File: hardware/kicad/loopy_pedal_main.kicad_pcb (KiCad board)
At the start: 2 copper layers, 175 x 118 mm, 88 parts, among them J1 USB_C_Receptacle_USB2.0_16P, J10 Conn_01x02, J2 Barrel_Jack, J3 Conn_01x06, J4 Conn_01x06, J5 Conn_01x08, J6 Conn_02x03_Odd_Even, J7 Conn_02x03_Odd_Even, J8 DIN-5_180degree, J9 DIN-5_180degree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

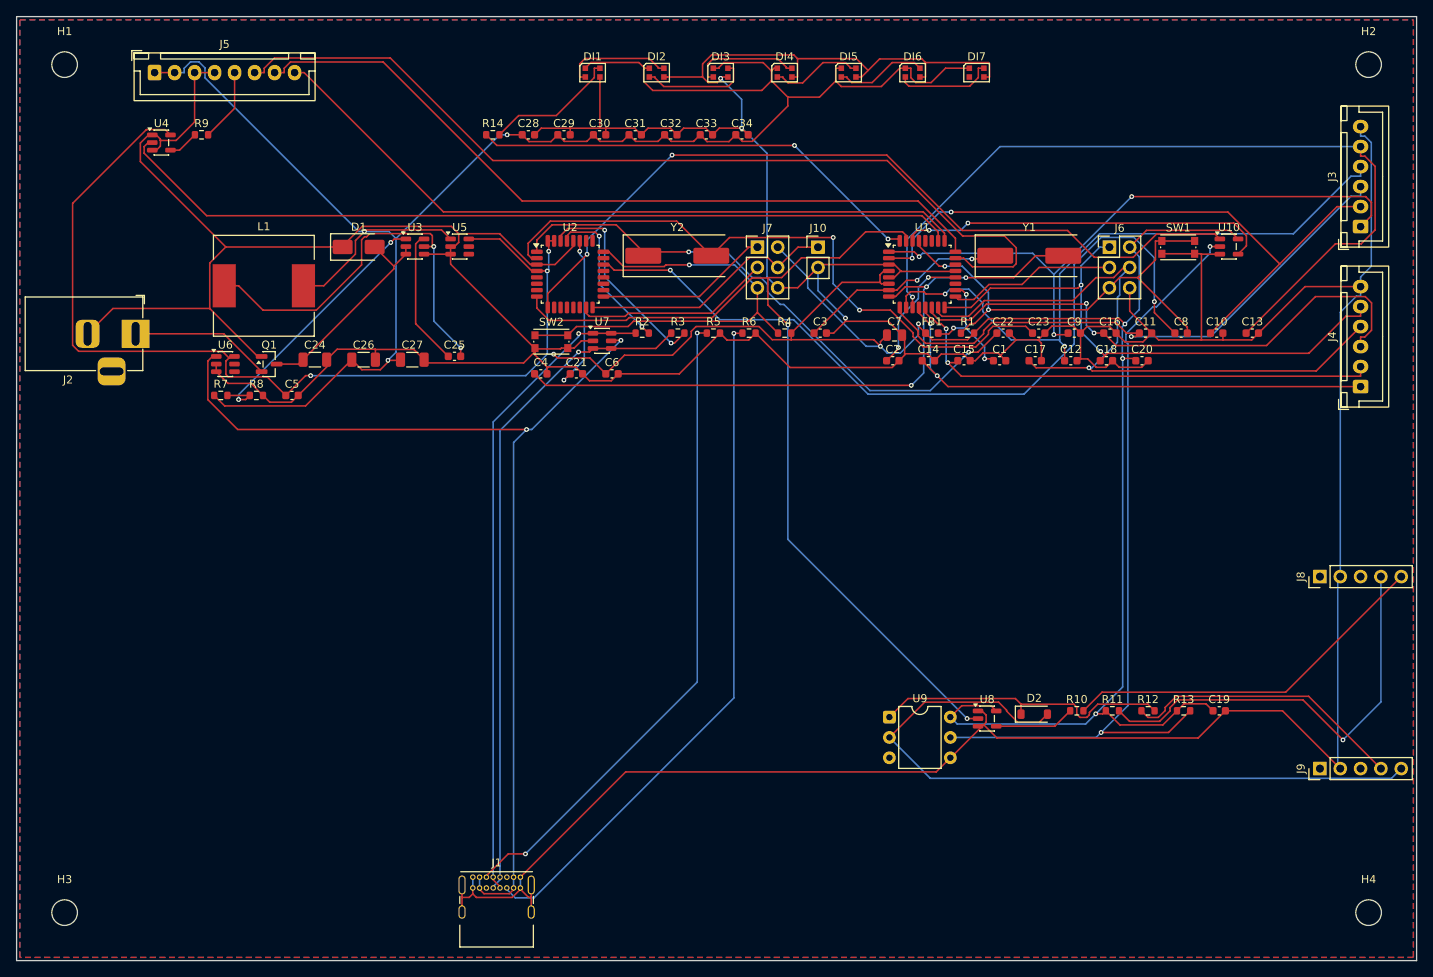
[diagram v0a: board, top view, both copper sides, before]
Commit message: refactor(pcb): compact main board 150x118 -> 145x74mm
Removed the large empty bottom-left quadrant by distributing connectors across
the bottom edge (USB-C + both MIDI DIN jacks) instead of stacking all four down
the right side, and tightening the functional zones. ~40% less board area.
Re-routed: 1137 segments / 95 vias, 0 DRC errors / 0 unrouted. Gerbers updated.
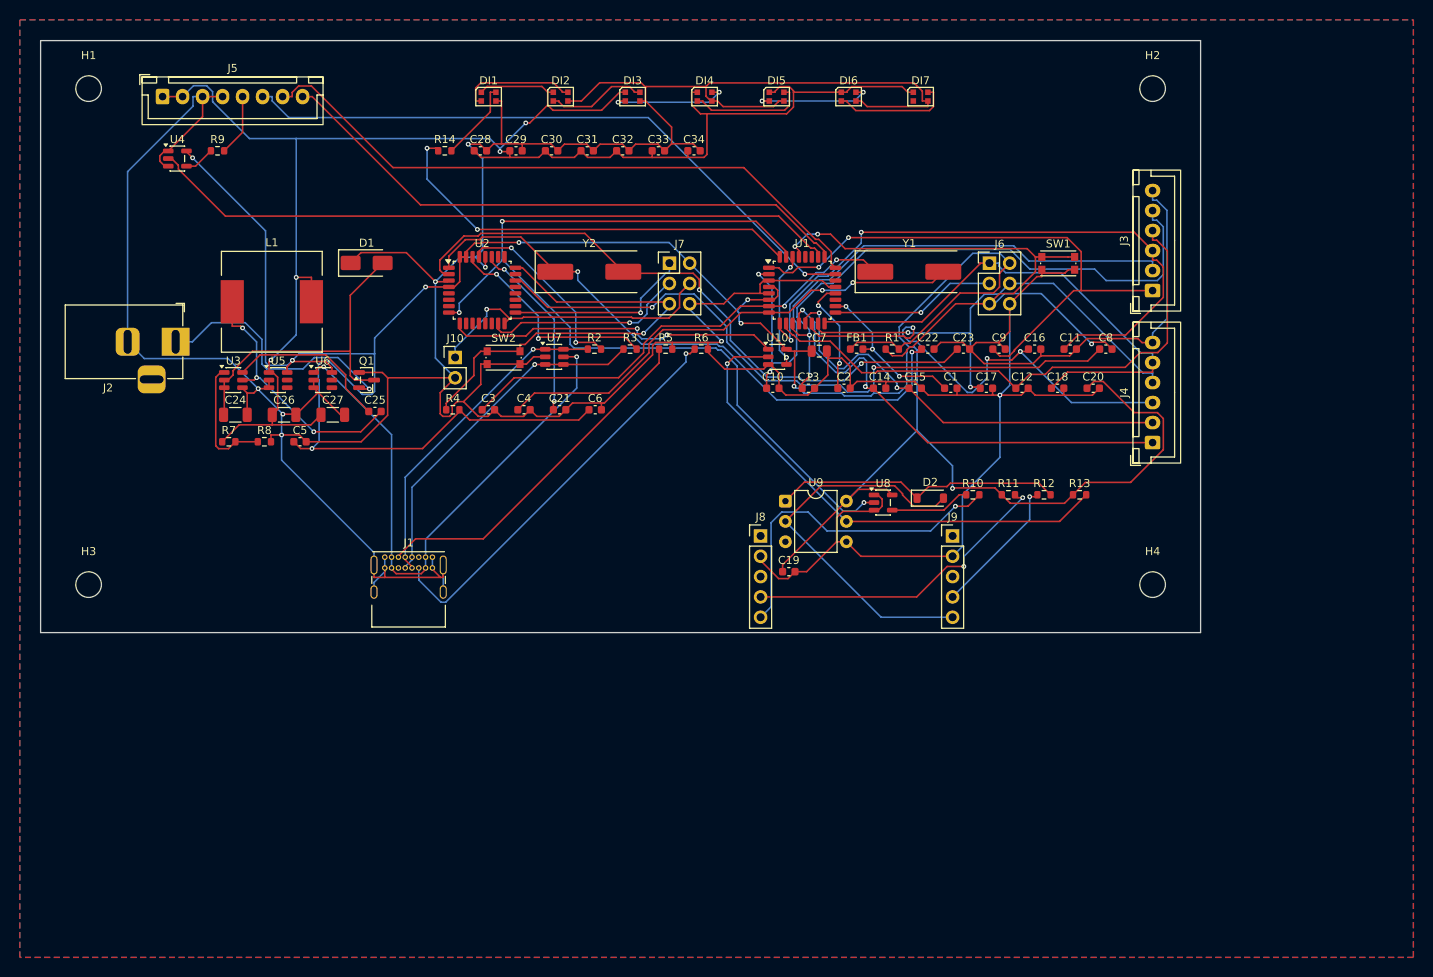
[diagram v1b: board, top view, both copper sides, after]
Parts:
- moved J8 70.1 mm to (118.0, 94.9), turned to 0 degrees
- moved U10 58.1 mm to (120.1, 72.5)
- moved C19 56.5 mm to (121.5, 99.4)
- moved C13 55.9 mm to (124.0, 76.5)
- moved C10 55.9 mm to (119.5, 76.5)
- moved J9 54.4 mm to (142.0, 94.9), turned to 0 degrees
- moved H4 49.1 mm to (167.0, 101.0)
- moved J10 47.4 mm to (79.8, 72.6)
- moved C3 42.6 mm to (84.0, 79.1)
- moved R4 42.6 mm to (79.5, 79.1)
- moved J1 41.5 mm to (71.0, 97.6)
- moved H3 41.1 mm to (34.0, 101.0)
- moved D2 30.0 mm to (139.2, 90.2)
- moved R10 30.0 mm to (144.5, 89.8)
- moved R11 30.0 mm to (149.0, 89.8)
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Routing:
- net GND: track 755.9 -> 650.9 mm, vias 3 -> 8
- net M16_TXD: track 100.7 -> 41.9 mm
- net VBUS: track 129.6 -> 71.1 mm
- net N$21: track 89.7 -> 49.0 mm
- net USB_D+: track 81.2 -> 41.2 mm
- net USB_D-: track 84.0 -> 44.0 mm
- net N$14: track 81.4 -> 44.5 mm, vias 2 -> 0
- net MIDI_IN_OPTO: track 99.4 -> 62.7 mm, vias 2 -> 1
- net ENC_A: track 116.3 -> 81.1 mm, vias 0 -> 1
- net N$15: track 86.0 -> 50.9 mm
- net UART_RX: track 46.4 -> 14.5 mm
- net N$3: track 26.7 -> 58.3 mm
- net SW_TRACK1: track 103.2 -> 73.9 mm, vias 1 -> 2
- net +5V_LED: track 238.0 -> 211.8 mm, vias 3 -> 4
- net SW_CLEAR: track 86.4 -> 60.9 mm, vias 1 -> 2
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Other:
- board size 175 x 118 mm -> 145 x 74 mm

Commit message: refactor(pcb): shrink main board to 100x98mm (fits 100x100 max)
Re-floorplanned from the 145x74 wide strip into a roughly square outline:
logic stacked in two rows, connectors distributed across all four edges
(barrel left; ring + indicator LEDs top; footswitch headers right; USB-C +
both MIDI DIN jacks bottom). Parts spread with wider gaps so Freerouting has
clean channels. Re-routed: 1091 segments / 78 vias, 0 DRC errors / 0 unrouted.
Gerbers + doc updated.
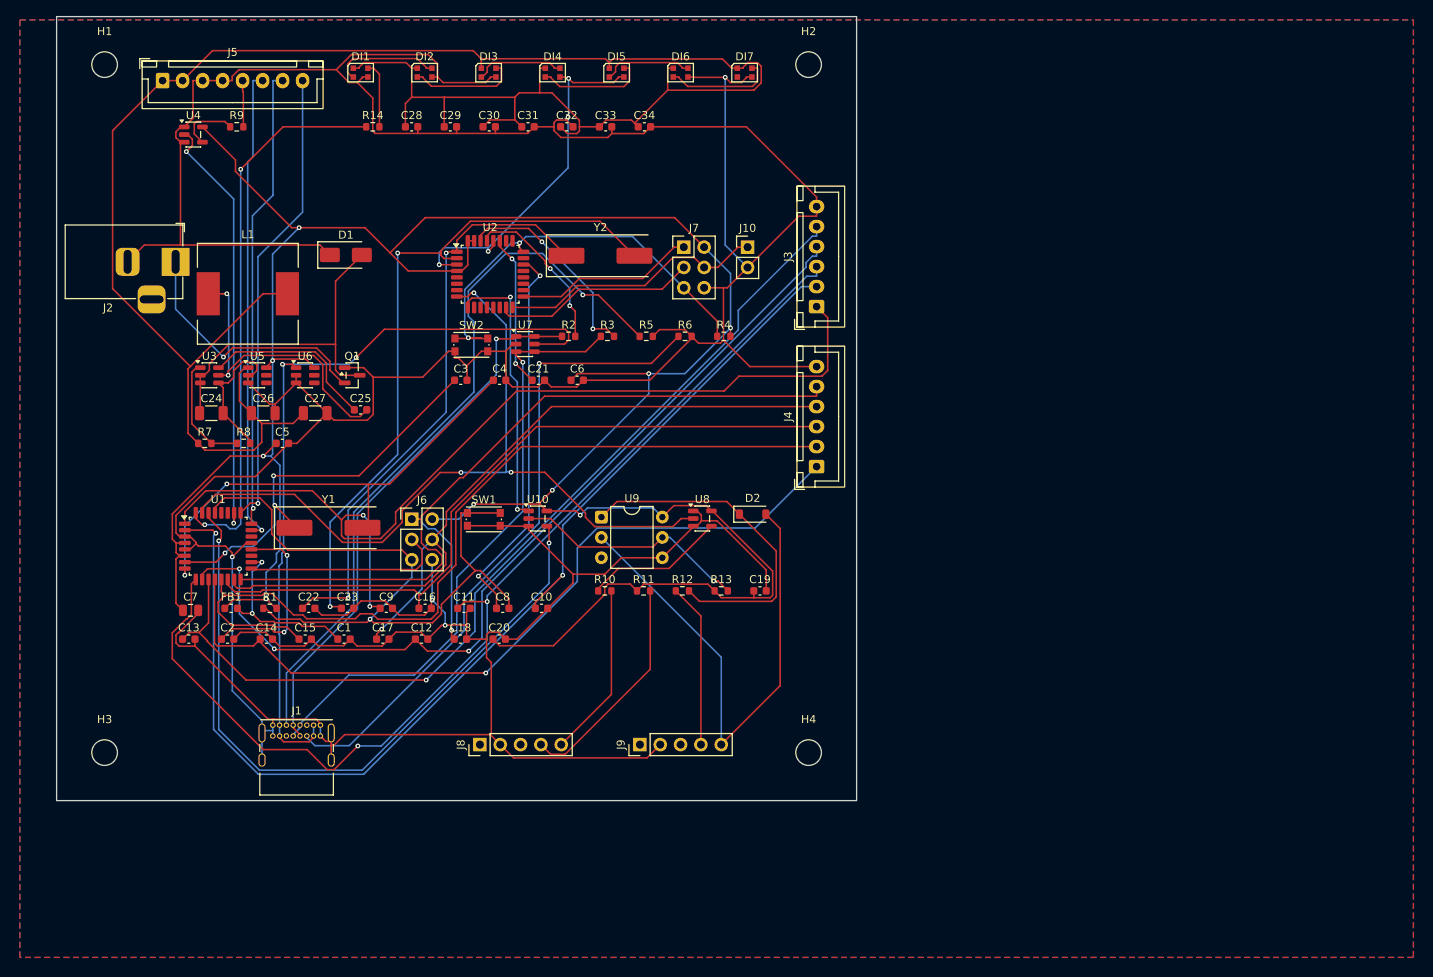
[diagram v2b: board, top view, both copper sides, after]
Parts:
- moved C7 85.0 mm to (46.7, 104.2)
- moved FB1 84.6 mm to (51.8, 104.0)
- moved R1 84.3 mm to (56.7, 104.0)
- moved C22 83.9 mm to (61.5, 104.0)
- moved C13 83.6 mm to (46.5, 107.8)
- moved C23 83.5 mm to (66.4, 104.0)
- moved C2 83.2 mm to (51.4, 107.8)
- moved C9 83.2 mm to (71.2, 104.0)
- moved C14 82.8 mm to (56.2, 107.8)
- moved C16 82.8 mm to (76.1, 104.0)
- moved C15 82.4 mm to (61.1, 107.8)
- moved C11 82.4 mm to (80.9, 104.0)
- moved C1 82.1 mm to (65.9, 107.8)
- moved C8 82.1 mm to (85.8, 104.0)
- moved C17 81.7 mm to (70.8, 107.8)
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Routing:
- net UART_RX: track 14.5 -> 88.2 mm
- net SW_STOP: track 76.3 -> 140.8 mm
- net +5V_LED: track 211.8 -> 264.6 mm, vias 4 -> 0
- net SW_TRACK3: track 54.5 -> 106.9 mm, vias 2 -> 0
- net SW_UNDO: track 79.9 -> 131.5 mm
- net SW_RECPLAY: track 70.5 -> 120.8 mm
- net GND: track 650.9 -> 698.5 mm
- net N$14: track 44.5 -> 92.0 mm, vias 0 -> 1
- net SW_BANK: track 65.0 -> 110.0 mm, vias 0 -> 1
- net SW_TRACK1: track 73.9 -> 117.6 mm, vias 2 -> 1
- net SW_MODE: track 69.0 -> 111.8 mm, vias 0 -> 3
- net SW_CLEAR: track 60.9 -> 103.7 mm, vias 2 -> 1
- net SW_TRACK2: track 58.2 -> 98.8 mm, vias 2 -> 1
- net DTR: track 84.9 -> 48.4 mm
- net RING_DATA: track 87.0 -> 53.3 mm, vias 0 -> 2
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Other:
- board size 145 x 74 mm -> 100 x 98 mm
